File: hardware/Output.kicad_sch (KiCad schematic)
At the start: 26 parts, among them J11 Conn_Coaxial, J12 Conn_Coaxial, J13 Conn_Coaxial, J14 Conn_Coaxial, J15 Conn_Coaxial, J16 Conn_Coaxial, J17 Conn_Coaxial, J18 Conn_Coaxial, U31 74LVCH2T45DC, U32 74LVCH2T45DC

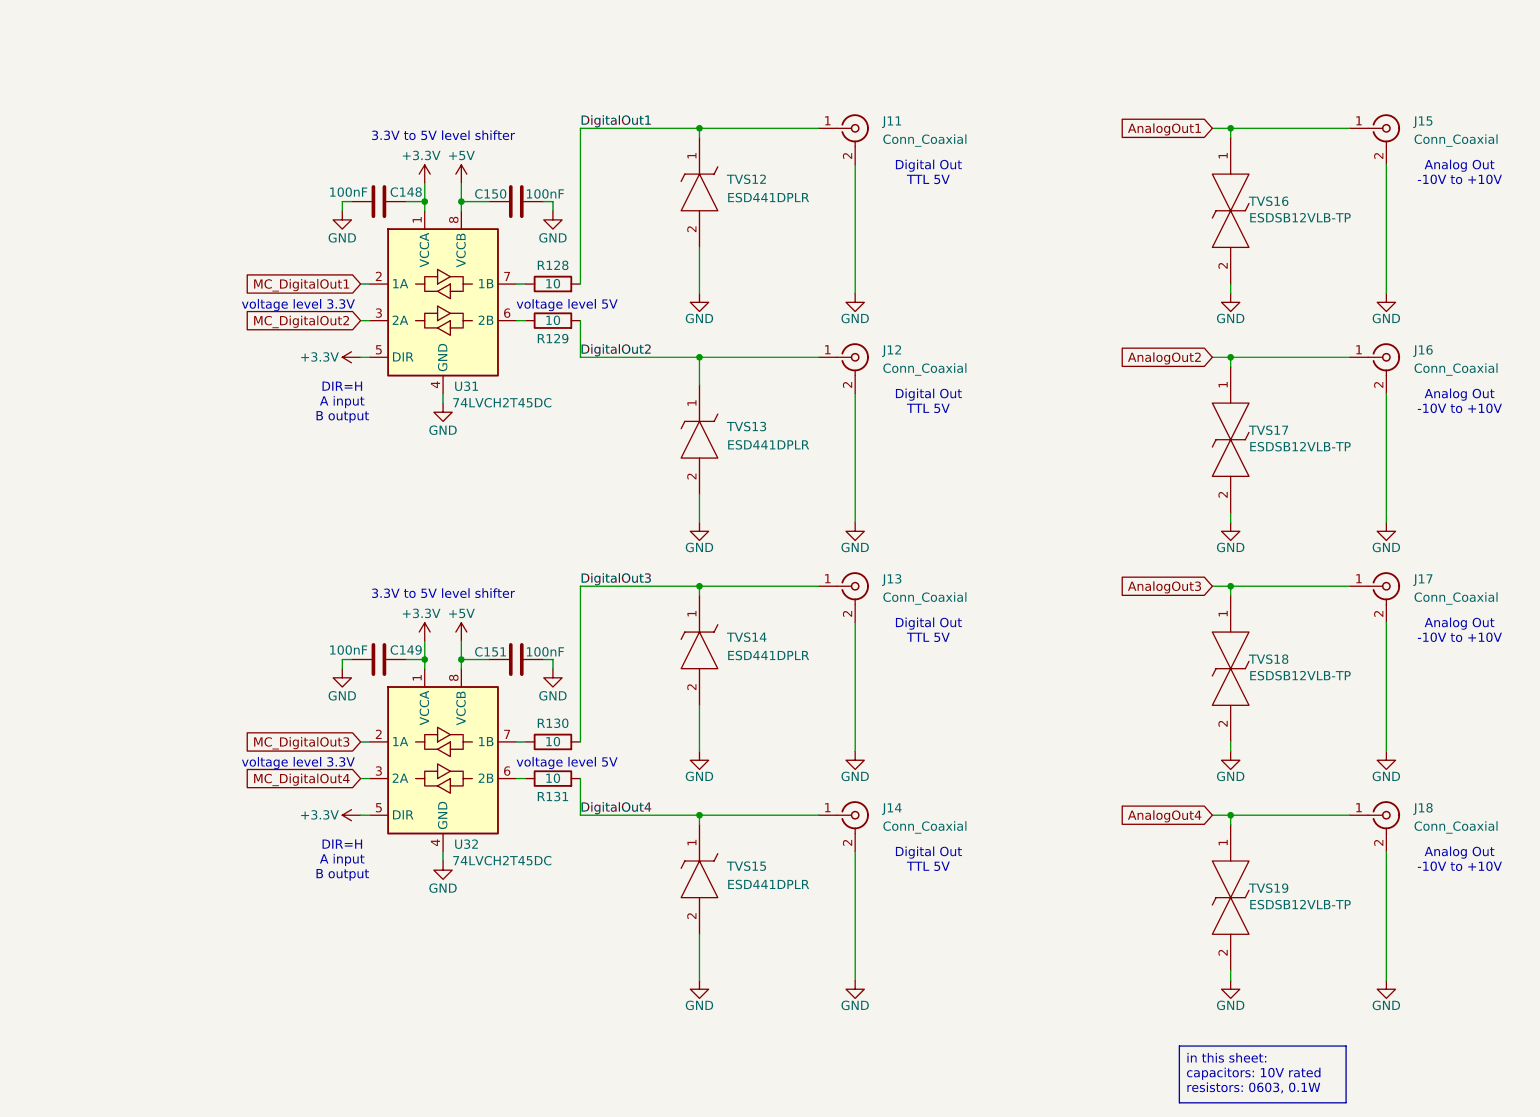
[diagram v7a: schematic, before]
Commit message: BOM for all capacitors and resistors is added correctly to the schematic
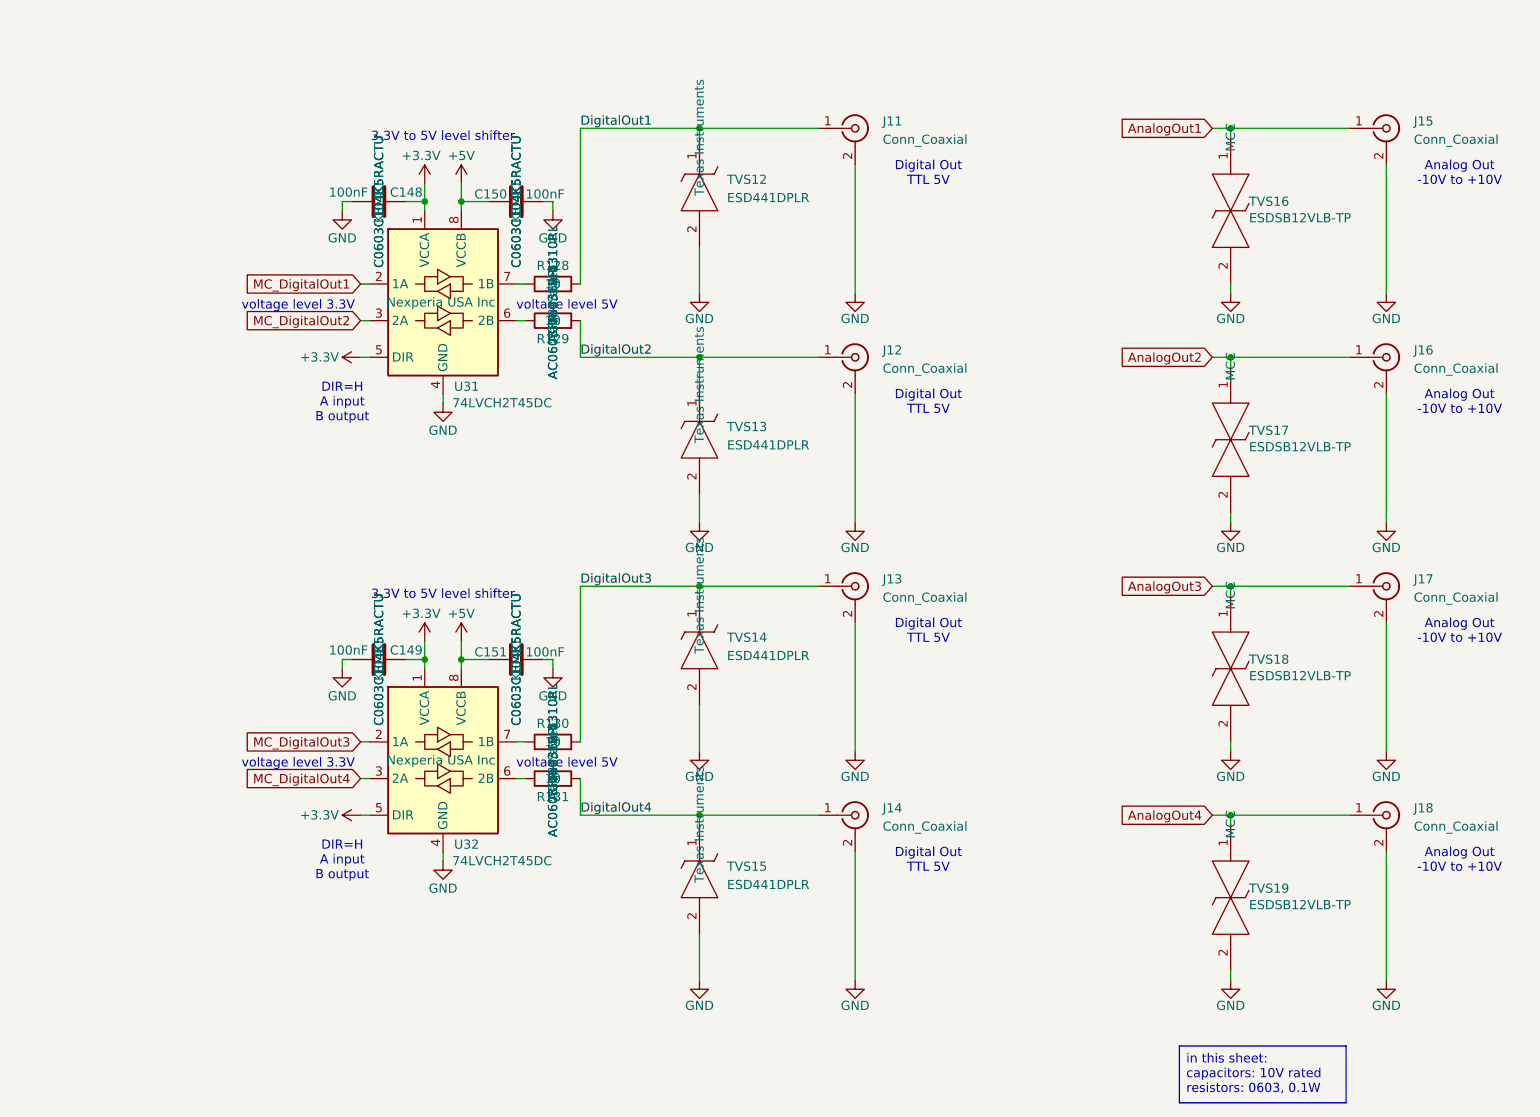
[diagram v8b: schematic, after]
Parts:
- C148, C149, C150, C151: Link https://www.digikey.com/en/products/detail/walsin-technolog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 -> https://www.digikey.com/en/products/detail/kemet/C0603C104K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; MPN (none) -> C0603C104K5RACTU; Manufacturer Walson Technology Corporation -> KEMET; Manufacturer Number 0402B104K160CT -> (none); Manufacturer_Name (none) -> KEMET; Manufacturer_Part_Number (none) -> C0603C104K5RACTU; Rated Voltage 16V -> 50V
- R128, R129, R130, R131: Link https://www.digikey.com/en/products/detail/yageo/SR0603FR-7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 -> https://www.digikey.com/en/products/detail/yageo/AC0603FR-1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; MPN (none) -> AC0603FR-1310RL; Manufacturer_Name (none) -> Yageo; Manufacturer_Part_Number (none) -> AC0603FR-1310RL
- TVS12, TVS13, TVS14, TVS15: Manufacturer (none) -> Texas Instruments
- TVS16, TVS17, TVS18, TVS19: Manufacturer (none) -> MCC
- U31, U32: Manufacturer_Name (none) -> Nexperia USA Inc.
